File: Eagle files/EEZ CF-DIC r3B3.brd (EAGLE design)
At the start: 155 x 85 mm, 242 parts, among them IC1 MC79L05, IC2 LP2951, IC3 VIPer35L, IC4 SI8233BB-D-IS1, IC5 LM5041B, IC6 IR11688STRPBF, IC7 TL072, IC8 TL103W, IC9 TL431, P1 T910W-50K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

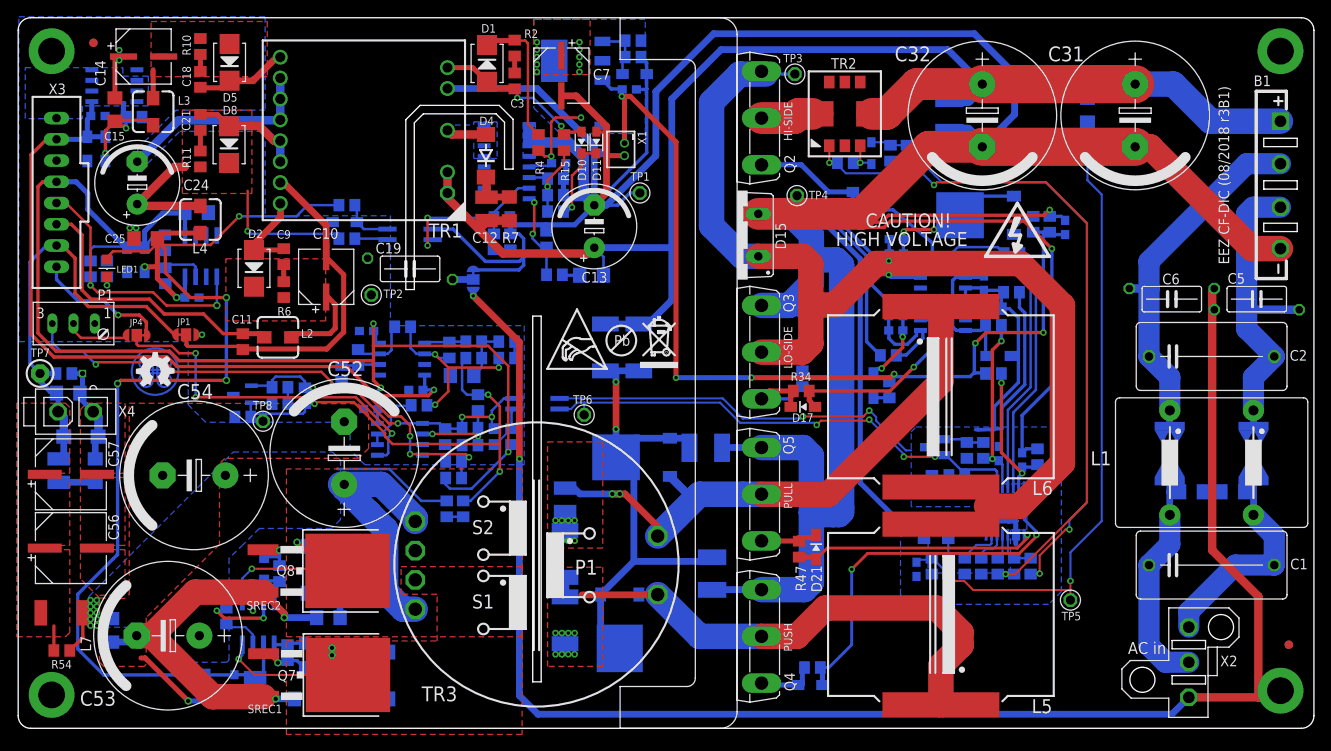
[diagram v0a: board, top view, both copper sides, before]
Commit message: Bridge rectifier relocated, Y2 capacitors optional positions added
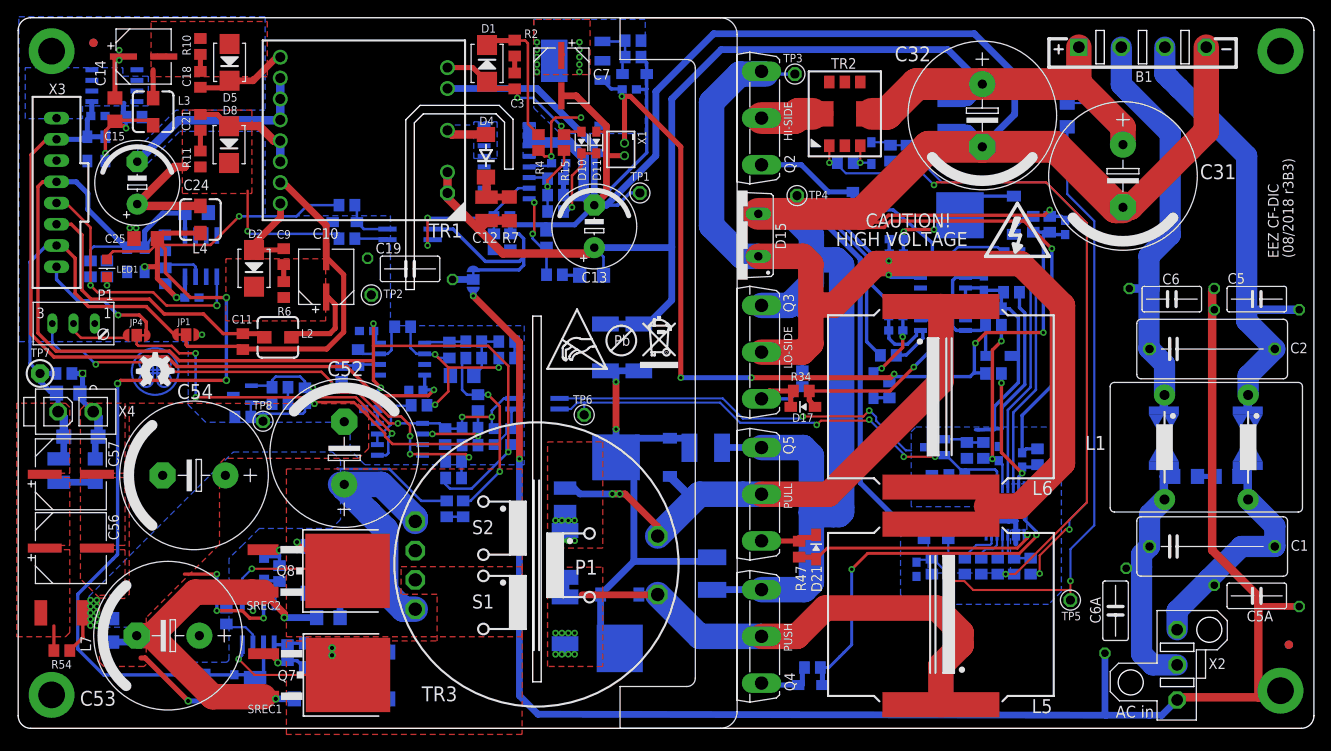
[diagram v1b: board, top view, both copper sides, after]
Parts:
- added C5A, C6A: N.C., EEZ_Lib1:CY075-032X103
- C1, C2: device rcl:C150-084X183 -> rcl:C150-072X183
- moved B1 23.3 mm to (139.5, 83.5), turned to 0 degrees
- moved C31 7.38 mm to (137.2, 68.1)
- moved SH1 7.38 mm to (137.2, 64.3), turned to 90 degrees
- moved R42 2.67 mm to (130.5, 69.9)
- moved R38 2.48 mm to (130.5, 75.4)
- moved C1 2.22 mm to (147.8, 23.7)
- moved SAR1 1.97 mm to (142.0, 36.7)
- moved SAR2 1.97 mm to (152.1, 36.7)
- moved R1 1.97 mm to (144.7, 32.1)
- moved R3 1.97 mm to (149.6, 32.1)
- moved L1 1.95 mm to (147.1, 35.6)
- moved X2 1.43 mm to (143.6, 9.59)
- moved C2 0.89 mm to (147.8, 47.4)
- moved C36 0.25 mm to (116.6, 75.3)
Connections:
- net N$28: now also C6A.2
- net N$30: now also C5A.2
- net PE: now also C5A.1, C6A.1
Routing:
- net N$24: track 38.5 -> 56.6 mm
- net PE: track 195.4 -> 207.8 mm
- net DC_BUS: track 179.3 -> 169.9 mm
- net GND: track 123.9 -> 132.2 mm, vias 11 -> 12
- net N$15: track 43.6 -> 50.1 mm
- net N$28: track 27.5 -> 31.5 mm
- net N$30: track 27.0 -> 30.7 mm
- net 0V: track 591.1 -> 592.3 mm
- net GNDA: track 22.5 -> 23.7 mm
- net ULVO: track 76.0 -> 75.1 mm
- net N$2: track 2.52 -> 3.09 mm
- net CT_OUT: track 76.2 -> 75.7 mm
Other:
- board text added: "(08/2018 r3B3)"
- board text added: "C5A"
- board text added: "C6A"
- board text added: "EEZ CF-DIC"
- board text removed: "EEZ CF-DIC (08/2018 r3B1)"
